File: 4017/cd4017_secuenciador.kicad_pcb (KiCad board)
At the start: 2 copper layers, 83.3 x 43.4 mm, 20 parts, among them J1 CLK_IN_555, J2 ALIM_EXT, J3 POT1_EXT, J4 POT2_EXT, J5 POT3_EXT, J6 POT4_EXT, J7 JACK_OUT, U1 CD4017BE

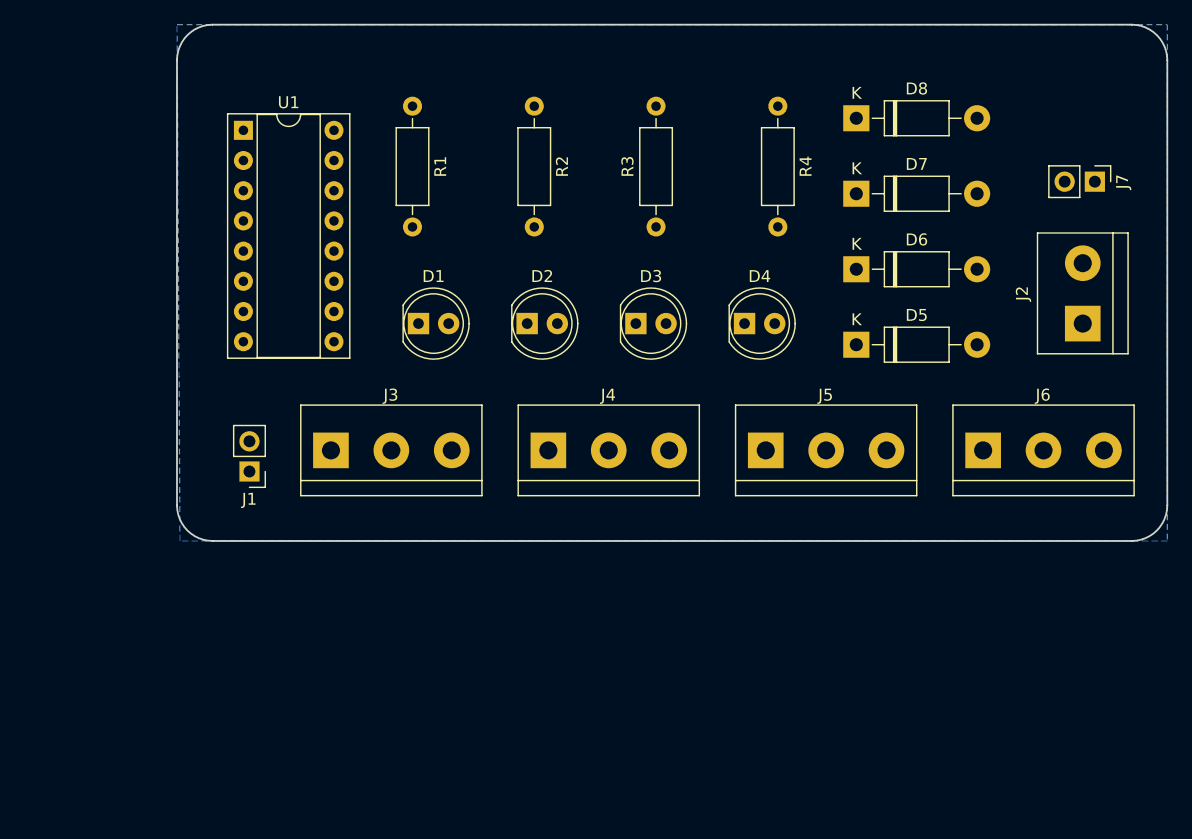
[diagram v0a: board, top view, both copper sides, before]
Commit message: enrutado 4017 + correccion esquematico
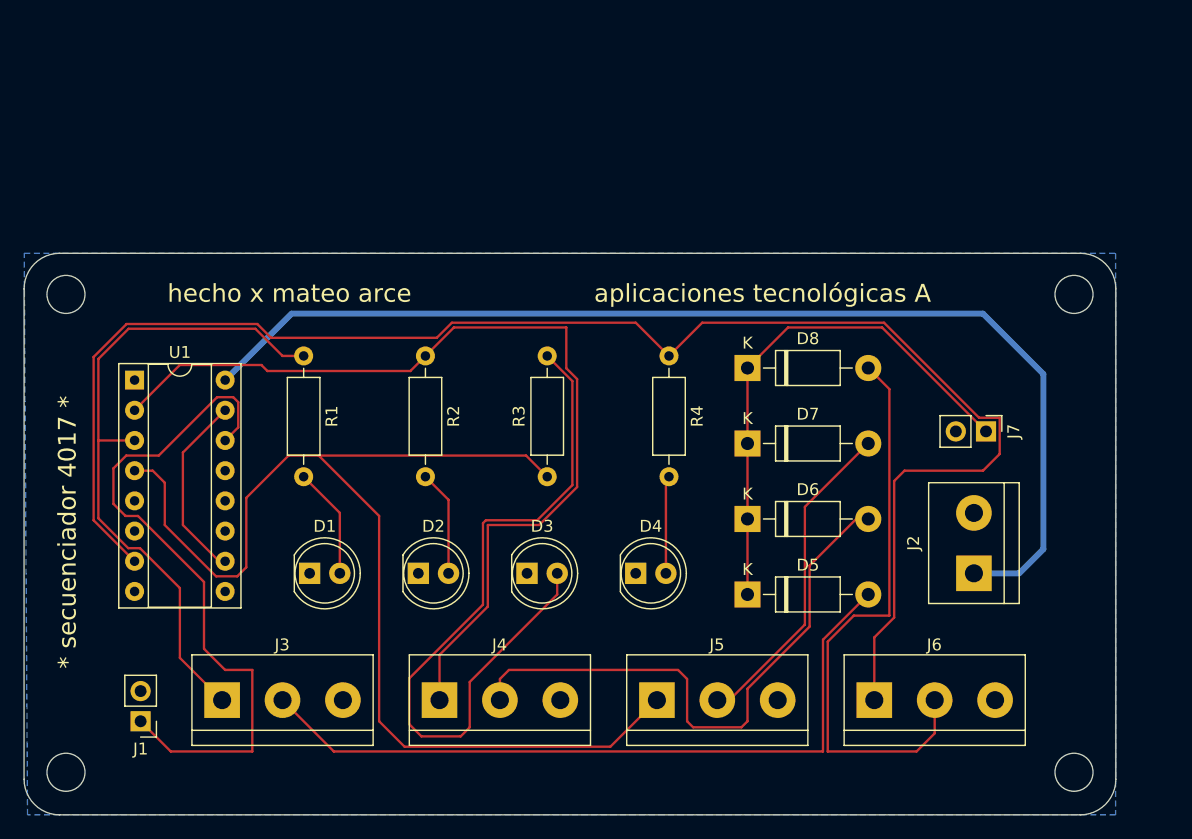
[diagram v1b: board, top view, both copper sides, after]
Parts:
- added REF**: MountingHole_3.2mm_M3, MountingHole:MountingHole_3.2mm_M3, F.Cu at (100.6, 118.0)
- added REF**: MountingHole_3.2mm_M3, MountingHole:MountingHole_3.2mm_M3, F.Cu at (185.4, 77.8)
- added REF**: MountingHole_3.2mm_M3, MountingHole:MountingHole_3.2mm_M3, F.Cu at (100.6, 77.8)
- added REF**: MountingHole_3.2mm_M3, MountingHole:MountingHole_3.2mm_M3, F.Cu at (185.4, 118.0)
- moved D2 22.9 mm to (130.3, 101.3)
- moved D3 22.9 mm to (139.4, 101.3)
- moved D4 22.9 mm to (148.6, 101.3)
- moved D5 22.9 mm to (158.0, 103.1)
- moved D6 22.9 mm to (158.0, 96.7)
- moved D7 22.9 mm to (158.0, 90.4)
- moved J1 22.9 mm to (106.9, 113.7)
- moved J7 22.9 mm to (178.0, 89.3)
- moved R1 22.9 mm to (120.6, 83.0)
- moved R2 22.9 mm to (130.9, 83.0)
- moved R3 22.9 mm to (141.1, 93.1)
- moved D1 22.9 mm to (121.1, 101.3)
- moved D8 22.9 mm to (158.0, 84.0)
- moved U1 22.9 mm to (106.4, 85.0)
- moved J3 22.9 mm to (113.8, 111.9)
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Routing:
- net Q3: track 0.00 -> 134.6 mm
- net Q2: track 0.00 -> 99.2 mm
- net VCC: track 0.00 -> 94.7 mm
- net Q1: track 0.00 -> 78.7 mm
- net Q0_WIPER: track 0.00 -> 62.0 mm
- net Q2_LEDA: track 0.00 -> 61.9 mm
- net CLK_IN: track 0.00 -> 57.9 mm
- net Q0: track 0.00 -> 55.9 mm
- net Q3_WIPER: track 0.00 -> 49.3 mm
- net Q1_WIPER: track 0.00 -> 49.0 mm
- net MIX_OUT: track 0.00 -> 44.2 mm
- net Q2_WIPER: track 0.00 -> 27.4 mm
- net Q4_RST: track 0.00 -> 15.9 mm
- net Q0_LEDA: track 0.00 -> 9.39 mm
- net Q1_LEDA: track 0.00 -> 8.93 mm
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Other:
- board size 83.3 x 43.4 mm -> 91.8 x 47.2 mm
- board text added: "* secuenciador 4017 *"
- board text added: "aplicaciones tecnológicas A"
- board text added: "hecho x mateo arce"
